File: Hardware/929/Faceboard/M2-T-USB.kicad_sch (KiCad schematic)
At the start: 31 parts, among them J3 Debug_4-2328724-5, P5 292_PWRCTL-50, P6 292_HIGH-SPEED-50, U10 CBTL04083ABS_518, U11 TS5USBC410YFFR, U12 Faceboard_Expander_FR2032IG56, U3 SN74CB3Q3245RGYR, U7 TCA9534

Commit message: Added components
ESD HDMI
Extra components planned
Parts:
- removed U11: TS5USBC410YFFR, Ziloo:TS5USBC410YFFR, symbol Ziloo:TS5USBC410YFFR
- removed U3: SN74CB3Q3245RGYR, Ziloo:SN74CB3Q3245RGYR, symbol Ziloo:SN74CB3Q3245PW
- added C1, C2: C, Capacitor_SMD:C_0402_1005Metric, symbol Device:C
- added D12, D13, D14, D15: D, Diode_SMD:D_0402_1005Metric, symbol Device:D
- added R6: 2M, Resistor_SMD:R_0402_1005Metric, symbol Device:R
- added R7: 1M, Resistor_SMD:R_0402_1005Metric, symbol Device:R
- added R8: 1K, Resistor_SMD:R_0402_1005Metric, symbol Device:R
- added U11: FSUSB42MUX, Package_SO:MSOP-10_3x3mm_P0.5mm, symbol Interface_USB:FSUSB42MUX
- added U2: SN74CBTLV3126PWR, Ziloo:SN74CBTLV3126PWR, symbol Ziloo:SN74CBTLV3126PWR
- added U3: TPS79633DCQ, Ziloo:TPS79633DCQ, symbol Ziloo:TPS79633DCQ
- added U4: TPS79618DCQR, Ziloo:TPS79618DCQR, symbol Ziloo:TPS79618DCQR
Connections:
- net NIGHT_I2C_SCL is gone; now on net POWER_SCL: P5.36 (POWER_SCL)
- net NIGHT_I2C_SDA is gone; now on net POWER_SDA: P5.35 (POWER_SDA)
- net B_USB_D+: now also U11.7 (HSD1+)
- net B_USB_D-: now also U11.6 (HSD1-)
- net CAM_3V3: now also U2.14 (VCC), U4.1 (EN), U4.2 (IN)
- net GND: now also R7.2, U11.10 (~{OE}), U11.5 (GND), U2.7 (GND), U3.3 (GND), U4.3 (GND)
- net LIVE_3V3: now also U11.1 (VCC), U3.4 (OUT)
- net MCU_SYS_INT: now also U12.13 (P4.1/XIN); no longer U12.25 (MCU_SYS_INT/A3/P1.3)
- net PD_USBC_INT: now also U12.18 (TA1.1/P4.0)
- net PWR_CHARGE: now also D12.1 (K)
- net SD2_nCD: no longer U12.38 (SD2_CD/P2.4)
- net SJTAG_MOD: now also J3.14
- net SPI2_SS0: no longer U12.37 (SPI2_SS0/P2.5)
- net STEM_I2C_SCL: now also U2.8 (3B)
- net STEM_I2C_SDA: now also U2.11 (4B)
- net STEM_INT: now also U12.12 (P4.2/XOUT); no longer U12.28 (STEM_INT/UCA0SIMO/A0/Vref-/P1.0)
- net SYS_I2C_SCL: now also U12.33 (UCB0CLK/SYS_SCL/P5.1), U2.3 (1B); no longer JP4.1 (A)
- net SYS_I2C_SDA: now also U12.34 (UCB0STE/SYS_SDA/P5.0), U2.6 (2B); no longer JP3.1 (A)
- net UART1_TXD: now also D14.2 (A)
- net UART2_RXD: now also J3.5, J3.6
- net UART4_RXD: now also J3.8
- net UART4_TXD: now also J3.9
- net USB2_DN: now also U11.4 (D-)
- net USB2_DP: now also U11.3 (D+)
- net at U7.1 (A0): now also R4.1; no longer R5.2
- net at U7.2 (A1): now also R5.2; no longer R4.1
- net at P5.6 (USB2_DP): now also U11.9 (HSD2+)
- net at P5.7 (USB2_DN): now also U11.8 (HSD2-)
- net VSOM: now reaches D6.2 (A), P6.26 (VSOM)
- net VSOM: now also D13.1 (K), U3.1 (EN), U3.2 (IN)
- net at D10.2 (A), P5.26 (VSOM): no longer U12.18 (TA1.1/P4.0)
- net at D8.2 (A), P5.15 (VSOM): no longer U12.19 (TA1.2/P8.3)
- net POWER_TO_SYS: now reaches U12.20 (TA1CLK/P8.2)
- net POWER_TO_SYS: now also U2.1 (1OE), U2.4 (2OE)
- net PD_HRESET: now reaches U12.35 (P2.7)
- net BAT_CE: now reaches U12.39 (P2.3)
- net BAT_CE: now also P5.24 (BAT_CE#)
- net POWER_SDA: now reaches U12.4 (P7.2)
- net POWER_SDA: now also U2.12 (4A), U2.5 (2A)
- net POWER_SCL: now reaches U12.5 (P7.1)
- net POWER_SCL: now also U2.2 (1A), U2.9 (3A)
- net USB_XD_SEL: now reaches U12.51 (SH2_STCP/P3.5)
- net USB_XD_SEL: now also P5.17 (USB_XD_SEL)
- net USB_XD_OE: now reaches U12.52 (SH1_STCP/P3.4)
- net USB_XD_OE: now also P5.16 (USB_XD_OE)
- net SHUTDOWN_BTN: now reaches U12.8 (P4.6)
- net SHUTDOWN_BTN: now also P5.27 (SHUTDOWN_BTN)
- net LOCK_BTN: now reaches U12.9 (P4.5)
- net LOCK_BTN: now also P5.28 (LOCK_BTN)
- net at P5.10 (USB1_SBU2): now also J3.29
- net BAT_INT: now reaches P5.23 (BAT_INT)
- net BAT_INT: now also JP4.1 (A)
- net BAT_EN: now reaches P5.25 (BAT_EN)
- net BAT_EN: now also U12.38 (P2.4)
- net at P5.44 (USB2_XDN): now also J3.27
- net at P5.45 (USB2_XDP): now also J3.26
- net HDMI_5V: now reaches P5.46 (5V)
- net at P5.47 (USB1_XDN): now also J3.25
- net at P5.48 (USB1_XDP): now also J3.24
- net at P5.9 (USB1_SBU1): now also J3.28
- net SYS_PD_CTL_INT: now reaches JP2.1 (A)
- net F_SBWTCK renamed FACE_SBWTCK
- net T-USB-EX_FW_RXD: no longer names the net of P6.28
- net T-USB-EX_FW_TXD: no longer names the net of P6.27
- net T_SBWTCK: no longer names the net of P6.21
- net T_SBWTDIO: no longer names the net of P6.23
- net UART1_RXD renamed FACE_FW_RXD
- new net: R6.2, R7.1, R8.1
- new net: D13.2 (A), D15.1 (K)
- new net: C1.1, U3.5 (NR/FB)
- new net: D12.2 (A), D14.1 (K)
- new net: C2.1, U4.5 (NR/FB)
- new net CAM_1V8: U4.4 (OUT)
- new net FACE_FW_TXD: U12.28 (FW_TXD/A0/Vref-/P1.0)
- new net POWER_PD_CTL_INT: JP3.1 (A)
- new net POWER_TO_STEM: U12.19 (TA1.2/P8.3), U2.10 (3OE), U2.13 (4OE)
- new net POWER_TO_SYS_STEM: U12.37 (P2.5)
- new net VSOM_LESS_1V4: D15.2 (A), U12.25 (VSOM_LESS_1V4/A3/P1.3)
- no-connect marks 3 -> 18
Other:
- note added: "SYS I2C Address: 0x26"
- note added: "debug ouput"
- note removed: "SYS I2C Address: 0x25 no good !! must be changed"
- note removed: "TODO protection/voltage translation in range of analog pin"
- moved on the sheet: D10, D8, R4, R5

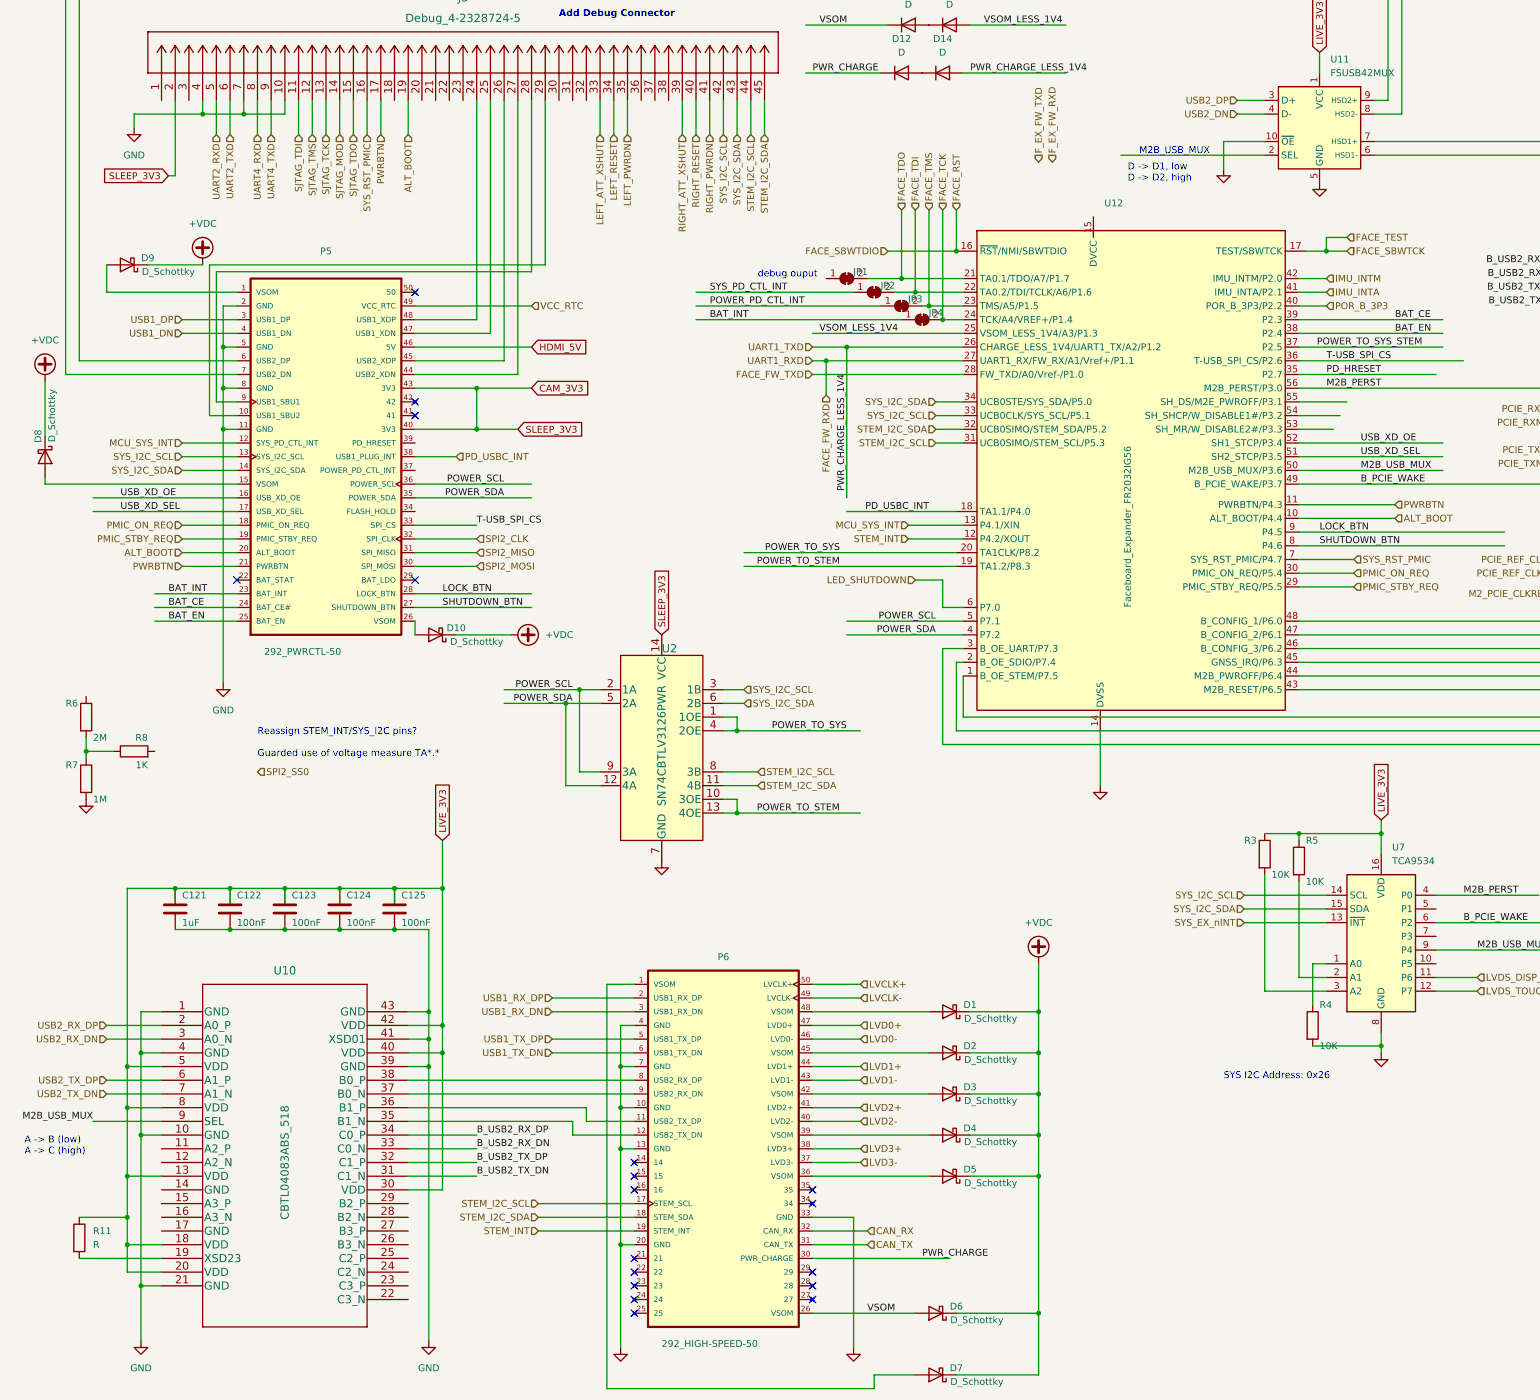
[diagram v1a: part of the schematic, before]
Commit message: Removed VSOM diodes
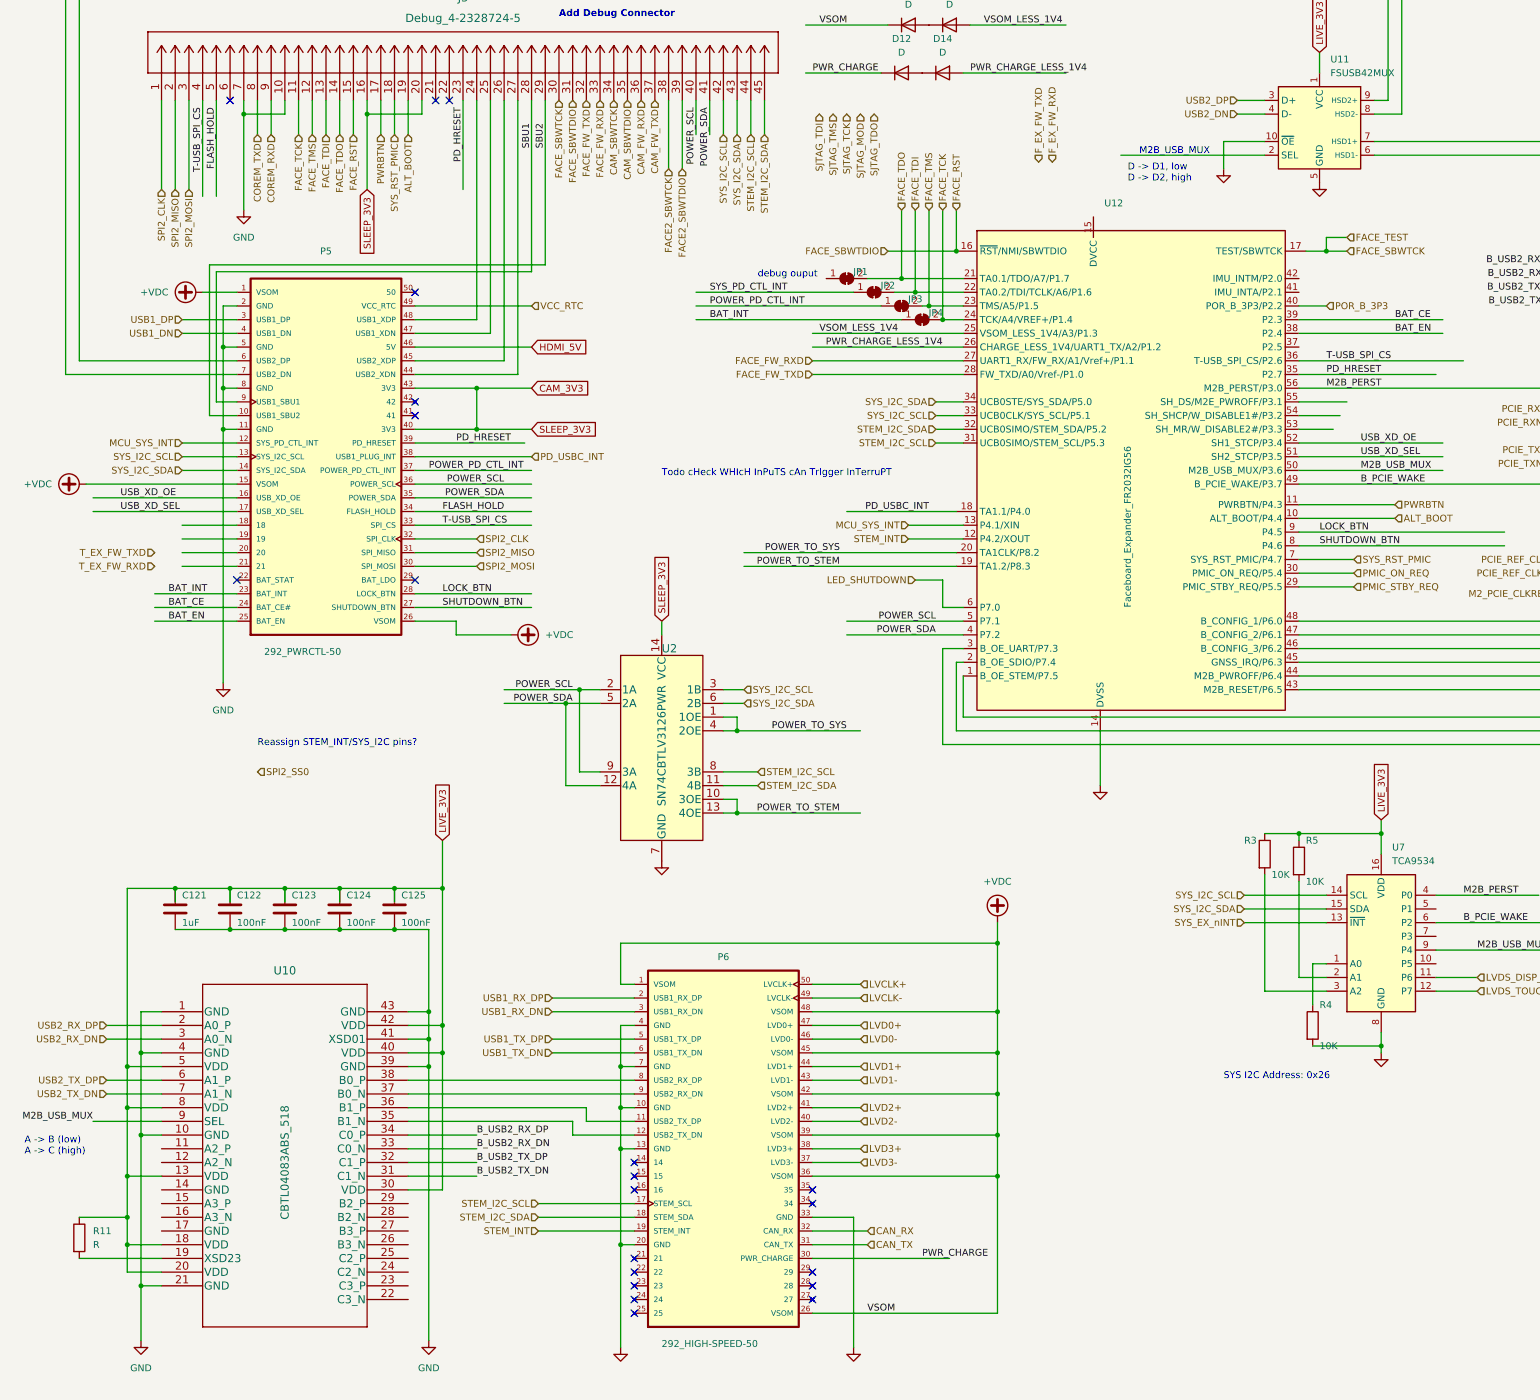
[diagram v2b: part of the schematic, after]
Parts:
- removed D1, D10, D2, D3, D4, D5, D6, D7, D8, D9: D_Schottky, Diode_SMD:D_SOD-123F, symbol Device:D_Schottky
- removed R6: 2M, Resistor_SMD:R_0402_1005Metric, symbol Device:R
- removed R7: 1M, Resistor_SMD:R_0402_1005Metric, symbol Device:R
- removed R8: 1K, Resistor_SMD:R_0402_1005Metric, symbol Device:R
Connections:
- net LEFT_ATT_XSHUT is gone; now on net FACE_FW_RXD: J3.33
- net RIGHT_PWRDN is gone; now on net POWER_SDA: J3.41
- net RIGHT_RESET is gone; now on net POWER_SCL: J3.40
- net VSOM is gone; now on net +VDC: D13.1 (K), P6.26 (VSOM), U3.1 (EN), U3.2 (IN)
- net +VDC: now also P5.1 (VSOM), P5.15 (VSOM), P5.26 (VSOM), P6.1 (VSOM), P6.36 (VSOM), P6.39 (VSOM), P6.42 (VSOM), P6.45 (VSOM), P6.48 (VSOM)
- net ALT_BOOT: no longer P5.20 (ALT_BOOT)
- net CAM_3V3: now also J3.16, J3.20; no longer J3.2
- net FACE_FW_TXD: now also J3.32
- net FACE_RST: now also J3.15, J3.31
- net FACE_SBWTCK: now also J3.30
- net FACE_TCK: now also J3.11
- net FACE_TDI: now also J3.13
- net FACE_TDO: now also J3.14
- net FACE_TMS: now also J3.12
- net GND: no longer J3.4
- net PD_HRESET: now also J3.23, P5.39 (PD_HRESET)
- net PMIC_ON_REQ: no longer P5.18 (PMIC_ON_REQ)
- net PMIC_STBY_REQ: no longer P5.19 (PMIC_STBY_REQ)
- net POWER_PD_CTL_INT: now also P5.37 (POWER_PD_CTL_INT)
- net PWRBTN: no longer P5.21 (PWRBTN)
- net SJTAG_MOD: no longer J3.14
- net SJTAG_TCK: no longer J3.13
- net SJTAG_TDI: no longer J3.11
- net SJTAG_TDO: no longer J3.15
- net SJTAG_TMS: no longer J3.12
- net SPI2_CLK: now also J3.1
- net SPI2_MISO: now also J3.2
- net SPI2_MOSI: now also J3.3
- net SYS_RST_PMIC: now also J3.18; no longer J3.16
- net T-USB_SPI_CS: now also J3.4
- net UART2_RXD: no longer J3.5, J3.6
- net SBU2: now reaches J3.29, P5.10 (USB1_SBU2)
- net FLASH_HOLD: now reaches P5.34 (FLASH_HOLD)
- net FLASH_HOLD: now also J3.5
- net SBU1: now reaches J3.28, P5.9 (USB1_SBU1)
- net CAM_FW_RXD: now reaches J3.36
- net CAM_FW_TXD: now reaches J3.37
- net FACE2_SBWTCK: now reaches J3.38
- net IMU_INTA: no longer names the net of U12.41 (IMU_INTA/P2.1)
- net IMU_INTM: no longer names the net of U12.42 (IMU_INTM/P2.0)
- net LEFT_PWRDN renamed CAM_SBWTDIO
- net LEFT_RESET renamed CAM_SBWTCK
- net POWER_TO_SYS_STEM: no longer names the net of U12.37 (P2.5)
- net RIGHT_ATT_XSHUT renamed FACE2_SBWTDIO
- net UART1_TXD renamed PWR_CHARGE_LESS_1V4
- net UART4_RXD renamed COREM_TXD
- net UART4_TXD renamed COREM_RXD
- no-connect marks 18 -> 21
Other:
- note added: "Reassign STEM_INT/SYS_I2C pins?"
- note added: "Todo cHeck WHIcH InPuTS cAn TrIgger InTerruPT"
- note removed: "Reassign STEM_INT/SYS_I2C pins? Guarded use of voltage measure TA*.*"

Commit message: PoC board task
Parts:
- removed C1: C, Capacitor_SMD:C_0402_1005Metric, symbol Device:C
- removed U3: TPS79633DCQ, Ziloo:TPS79633DCQ, symbol Ziloo:TPS79633DCQ
- added J7: USB_B_Micro, Connector_USB:USB_Micro-B_Wuerth_629105150521, symbol Connector:USB_B_Micro
- added R19, R20, R21, R22, R6, R8: 0R, Resistor_SMD:R_0402_1005Metric, symbol Device:R
- added R7: DNP, Resistor_SMD:R_0402_1005Metric, symbol Device:R
- added SW1: Reset, Button_Switch_SMD:SW_SPST_EVQP7A, symbol Switch:SW_Push
- added SW2: Power, Button_Switch_SMD:SW_SPST_EVQP7A, symbol Switch:SW_Push
- added SW3: Alt. Boot, Button_Switch_SMD:SW_SPST_EVQP7A, symbol Switch:SW_Push
- added SW4: Power, Connector_PinHeader_2.54mm:PinHeader_2x06_P2.54mm_Vertical_SMD, symbol Connector_Generic:Conn_02x06_Odd_Even
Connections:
- net SYS_EX_nINT is gone; now on net PD_USBC_INT: U7.13 (~{INT})
- net ALT_BOOT: now also R20.1
- net CAM_3V3: now also SW4.9 (Pin_9); no longer P5.40 (3V3), P5.43 (3V3)
- net GND: now also P6.16 (GND), P6.23 (GND), J7.5 (GND), J7.6 (Shield), R21.2, R8.2, SW4.11 (Pin_11), SW4.12 (Pin_12)
- net HDMI_5V: now also SW4.5 (Pin_5); no longer P5.46 (5V)
- net LIVE_3V3: now also R22.1, SW4.7 (Pin_7)
- net POR_B_3P3: now also R7.1
- net PWRBTN: now also R19.1
- net SYS_RST_PMIC: now also R6.1
- net +VDC renamed VSOM_TU
- net VSOM_TU: now also SW4.2 (Pin_2), SW4.4 (Pin_4); no longer D13.1 (K)
- net VCC_RTC renamed VCC_RTC_TU
- net VCC_RTC_TU: now also SW4.10 (Pin_10)
- new net: R20.2, SW3.1
- new net: R22.2, SW3.2
- new net: R6.2, R7.2, SW1.1
- new net: R21.1, SW2.2
- new net: R19.2, SW2.1
- new net: R8.1, SW1.2
- new net 3V3_TU: P5.40 (3V3), P5.43 (3V3), SW4.8 (Pin_8)
- new net 5V_TU: P5.46 (5V), SW4.6 (Pin_6)
- new net VSOM: D13.1 (K), SW4.1 (Pin_1), SW4.3 (Pin_3)
- no-connect marks 21 -> 19
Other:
- note added: "TODO MSG RX/TX"
- note added: "TODO revise if CAM voltage is live or sleep"
- note added: "TODO upregulate VSOM to 5.1V 2A"
- moved on the sheet: C121, C122, C123, C124, C125, R11, R3, R4, R5, U10, U7
